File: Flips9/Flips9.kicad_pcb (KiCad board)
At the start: 2 copper layers, 100 x 100 mm, 45 parts, among them CN1 UFP2810, U1 74238, U11 74238, U12 74238, U13 TD62783, U14 ULN2803/2003, U21 74238, U22 74238, U23 TD62783, U24 ULN2803/2003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

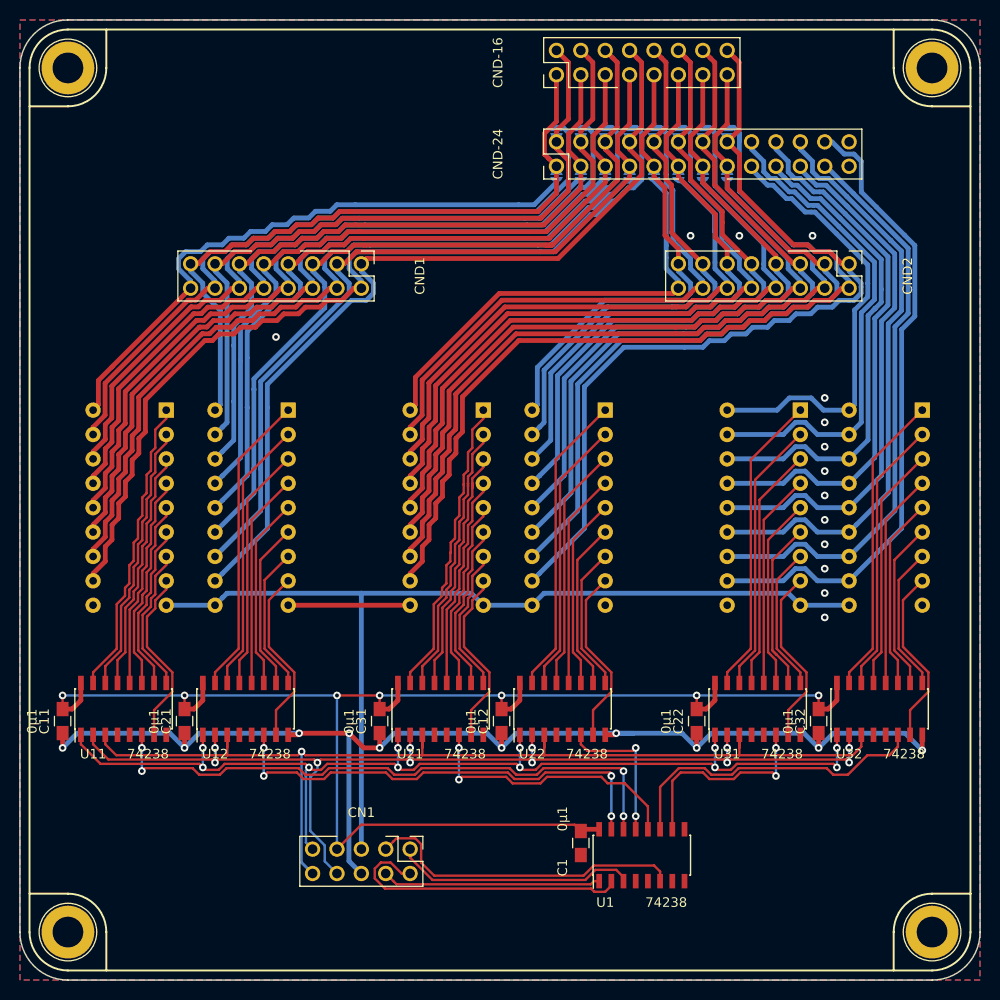
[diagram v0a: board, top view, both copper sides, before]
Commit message: adding rows 25-32
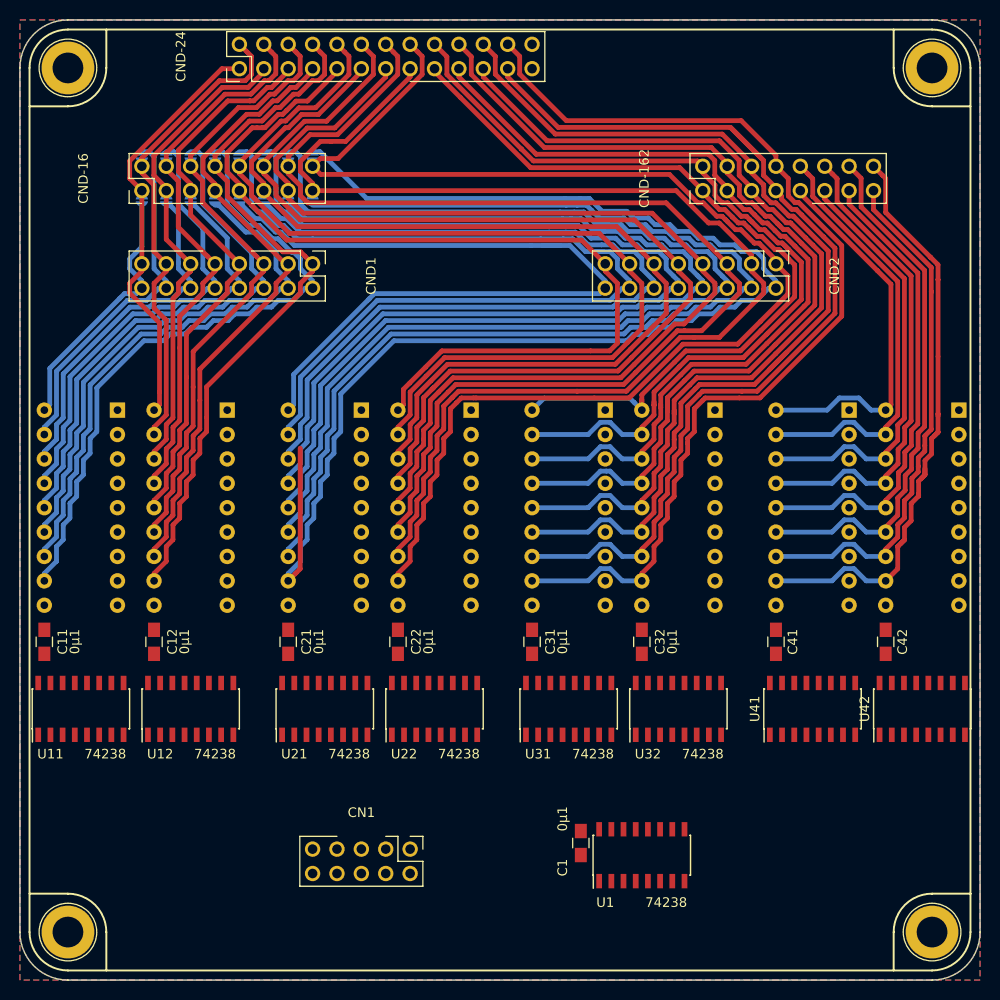
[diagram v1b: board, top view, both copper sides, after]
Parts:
- added C41: 0μ1, Capacitors_SMD:C_0805_HandSoldering, F.Cu at (129.5, 115.6)
- added C42: 0μ1, Capacitors_SMD:C_0805_HandSoldering, F.Cu at (141.0, 115.6)
- added CND-162: Conn_02x08_Odd_Even, Own:Pin_Header_Straight_Shrouded_Locks_2x08_Pitch2.54mm_ConvNumbering, F.Cu at (121.9, 68.6)
- added U41: 74238, Housings_SOIC:SOIC-16_3.9x9.9mm_Pitch1.27mm, F.Cu at (133.3, 122.6)
- added U42: 74238, Housings_SOIC:SOIC-16_3.9x9.9mm_Pitch1.27mm, F.Cu at (144.8, 122.6)
- added U43: TD62783, Housings_DIP:DIP-18_W7.62mm_Socket, B.Cu at (137.2, 91.4)
- added U44: ULN2803/2003, Housings_DIP:DIP-18_W7.62mm_Socket, B.Cu at (148.6, 91.4)
- moved CND-16 44.8 mm to (63.5, 68.6)
- moved JP101 43.3 mm to (63.5, 69.6)
- moved JP102 43.3 mm to (63.5, 65.0)
- moved JP105 43.3 mm to (68.6, 69.6)
- moved JP106 43.3 mm to (68.6, 65.0)
- moved JP109 43.3 mm to (73.7, 69.6)
- moved JP110 43.3 mm to (73.7, 65.0)
- moved JP113 43.3 mm to (78.7, 69.6)
- moved JP114 43.3 mm to (78.7, 65.0)
- moved JP103 43.3 mm to (66.0, 69.6)
- moved JP104 43.3 mm to (66.0, 65.0)
- moved JP107 43.3 mm to (71.1, 69.6)
- moved JP108 43.3 mm to (71.1, 65.0)
- moved JP111 43.3 mm to (76.2, 69.6)
- moved JP112 43.3 mm to (76.2, 65.0)
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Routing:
- net VCC: track 156.5 -> 0.00 mm, vias 7 -> 0
- net GND: track 140.2 -> 0.00 mm, vias 24 -> 0
- net /UnitY/A2: track 110.8 -> 0.00 mm, vias 1 -> 0
- net /UnitY/A0: track 109.5 -> 0.00 mm, vias 11 -> 0
- net /UnitY/A1: track 109.3 -> 0.00 mm, vias 11 -> 0
- net +24V: track 99.9 -> 0.00 mm
- net /Y32: track 0.00 -> 63.8 mm
- net /UnitY/E0H: track 62.5 -> 0.00 mm, vias 4 -> 0
- net /Y30: track 0.00 -> 55.5 mm
- net /Y31: track 0.00 -> 55.0 mm
- net /Y28: track 0.00 -> 50.3 mm
- net /Y29: track 0.00 -> 49.9 mm
- net /SX16: track 91.9 -> 141.2 mm
- net /UnitY/E0L: track 48.1 -> 0.00 mm, vias 4 -> 0
- net /Y15: track 81.0 -> 128.3 mm
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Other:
- board text added: "UDN2981 can replace TD62783"
- board text removed: "ULN2003 can replace ULN2803 (ULN2803 pins 1+18 unused) UDN2981 can replace TD62783"

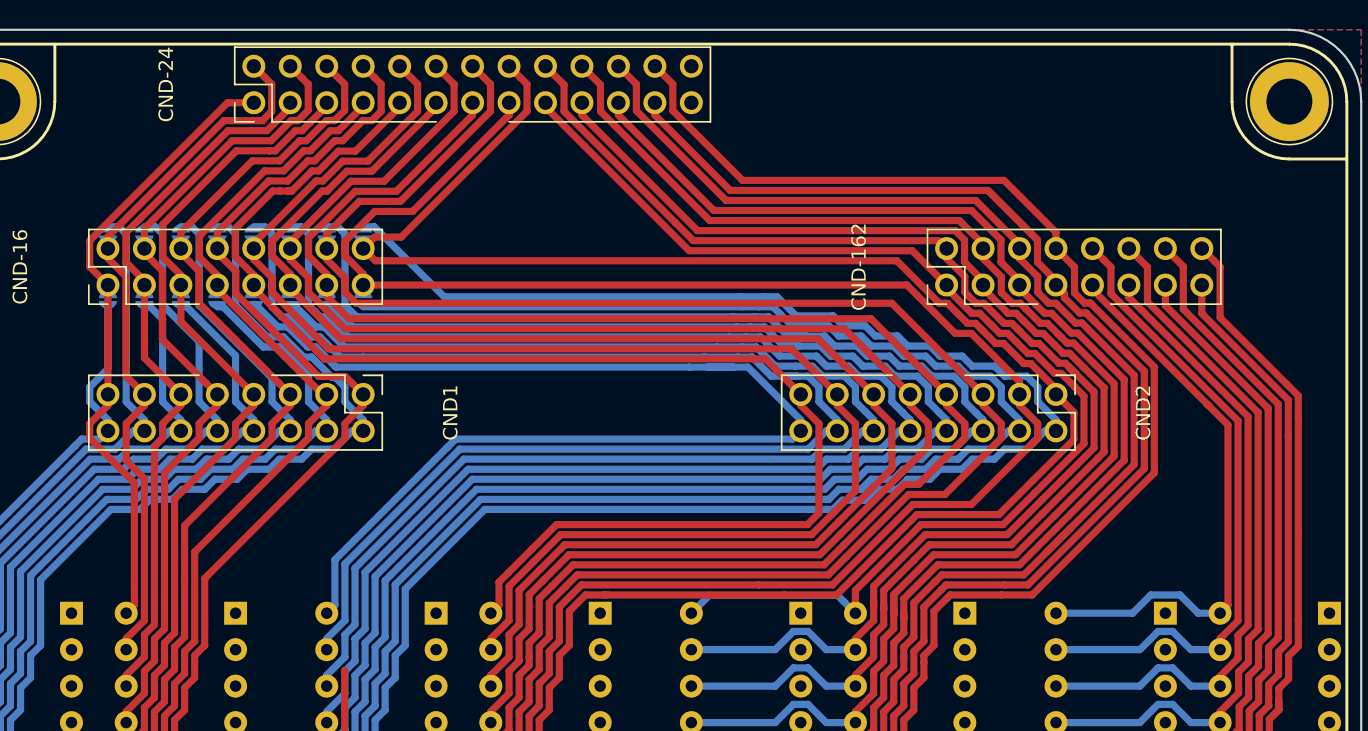
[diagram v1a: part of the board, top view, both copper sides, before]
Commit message: compactify driver traces
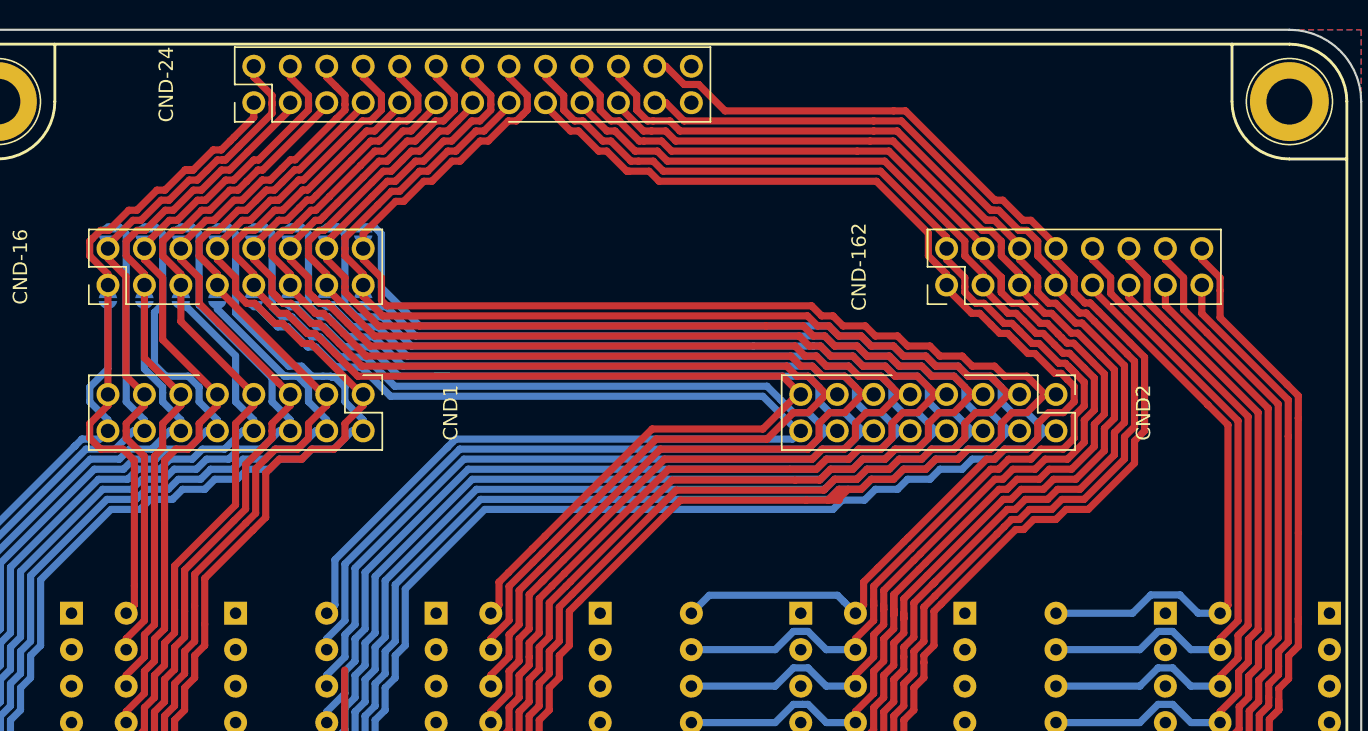
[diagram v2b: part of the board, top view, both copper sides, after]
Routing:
- net /Y23: track 104.7 -> 97.7 mm
- net /Y9: track 96.6 -> 90.1 mm
- net /Y10: track 104.6 -> 99.1 mm
- net /Y11: track 105.8 -> 101.5 mm
- net /Y12: track 114.2 -> 110.8 mm
- net /Y13: track 116.9 -> 113.5 mm
- net /Y24: track 105.6 -> 102.3 mm
- net /Y15: track 128.3 -> 125.0 mm
- net /SX16: track 141.2 -> 143.8 mm
- net /Y14: track 125.5 -> 122.9 mm
- net /Y22: track 102.7 -> 100.2 mm
- net /Y7: track 67.3 -> 69.6 mm
- net /SX9: track 84.5 -> 82.2 mm
- net /Y19: track 90.4 -> 88.2 mm
- net /Y21: track 95.3 -> 93.2 mm
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
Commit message: finish routing
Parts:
- moved CN1 14.6 mm to (106.0, 137.2)
- moved C1 8.70 mm to (116.8, 132.3), turned to 90 degrees
- moved U1 6.10 mm to (121.7, 138.0)
- moved C11 1.27 mm to (53.3, 116.8)
- moved C12 1.27 mm to (64.8, 116.8)
- moved C21 1.27 mm to (78.7, 116.8)
- moved C22 1.27 mm to (90.2, 116.8)
- moved C31 1.27 mm to (104.1, 116.8)
- moved C32 1.27 mm to (115.6, 116.8)
- moved C41 1.27 mm to (129.5, 116.8), turned to 90 degrees
- moved C42 1.27 mm to (141.0, 116.8), turned to 90 degrees
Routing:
- net GND: track 0.00 -> 811.3 mm, vias 0 -> 56
- net VCC: track 0.00 -> 236.2 mm, vias 0 -> 9
- net /UnitY/A2: track 0.00 -> 122.2 mm, vias 0 -> 8
- net /UnitY/A1: track 0.00 -> 120.5 mm, vias 0 -> 8
- net /UnitY/A0: track 0.00 -> 113.2 mm, vias 0 -> 9
- net +24V: track 0.00 -> 109.0 mm, vias 0 -> 1
- net /UnitY/E0H: track 0.00 -> 70.4 mm, vias 0 -> 2
- net /UnitY/E0L: track 0.00 -> 58.4 mm, vias 0 -> 2
- net /UnitY/E1H: track 0.00 -> 47.0 mm, vias 0 -> 2
- net /UnitY/E1L: track 0.00 -> 34.7 mm, vias 0 -> 2
- net /UnitY/E3L: track 0.00 -> 31.8 mm, vias 0 -> 2
- net Net-(U42-Pad15): track 0.00 -> 31.3 mm
- net Net-(U32-Pad15): track 0.00 -> 31.3 mm
- net Net-(U31-Pad15): track 0.00 -> 31.3 mm
- net Net-(U22-Pad15): track 0.00 -> 31.3 mm
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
